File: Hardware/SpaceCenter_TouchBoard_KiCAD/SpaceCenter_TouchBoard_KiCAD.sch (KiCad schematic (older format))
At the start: 6 parts, among them J1 Conn_01x05_Male, J2 TOUCH_SENSOR

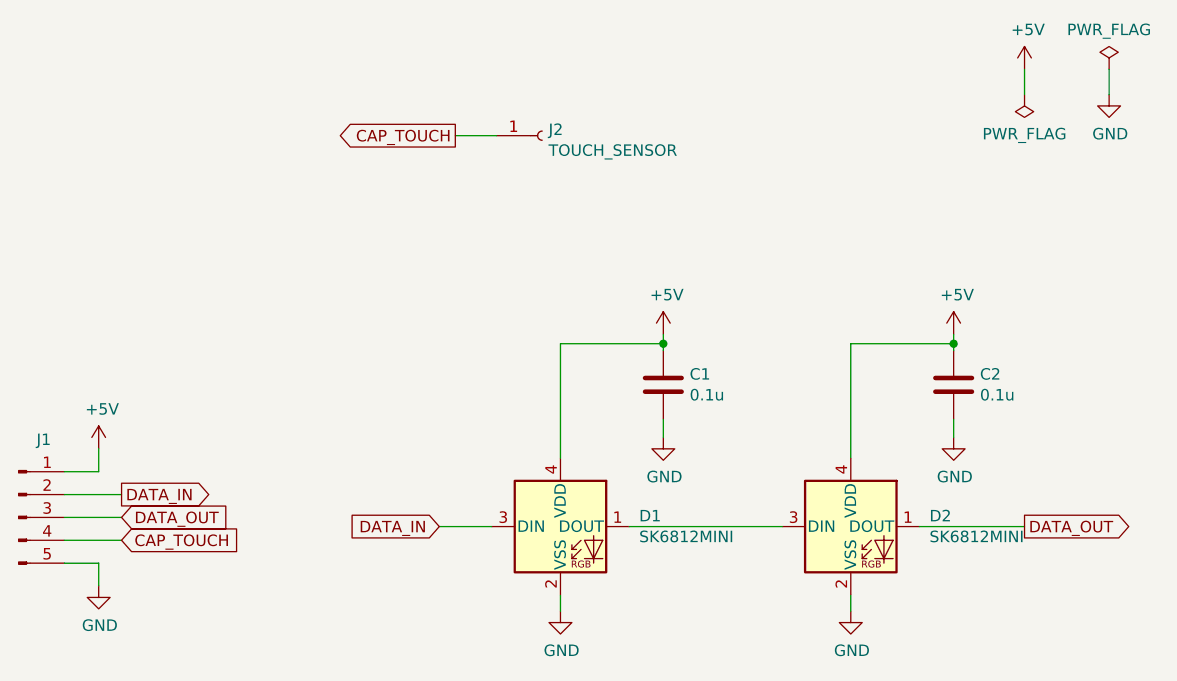
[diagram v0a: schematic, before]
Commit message: TouchBoard updated and ordered
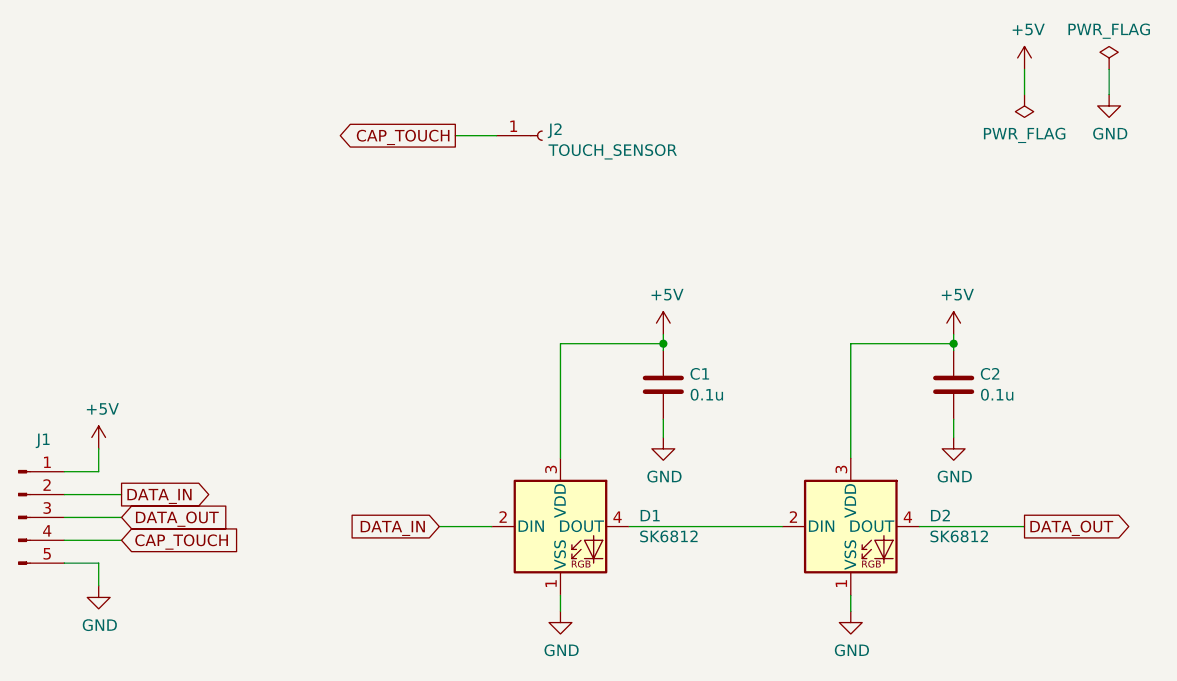
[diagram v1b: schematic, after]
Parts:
- removed D1, D2: SK6812MINI, LED_SMD:LED_SK6812MINI_PLCC4_3.5x3.5mm_P1.75mm, symbol LED:SK6812MINI
- added D1, D2: SK6812, LED_SMD:LED_SK6812_PLCC4_5.0x5.0mm_P3.2mm, symbol LED:SK6812
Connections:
- net +5V: now also D1.3 (VDD), D2.3 (VDD)
- net DATA_IN: now also D1.2 (DIN)
- net DATA_OUT: now also D2.4 (DOUT)
- net GND: now also D1.1 (VSS), D2.1 (VSS)
- new net: D1.4 (DOUT), D2.2 (DIN)
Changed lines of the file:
@@
 $EndDescr
-$Comp
-L LED:SK6812MINI D1
-U 1 1 5F27FCDA
-P 6030 4000
-F 0 "D1" H 6374 4046 50  0000 L CNN
-F 1 "SK6812MINI" H 6374 3955 50  0000 L CNN
-F 2 "LED_SMD:LED_SK6812MINI_PLCC4_3.5x3.5mm_P1.75mm" H 6080 3700 50  0001 L TNN
-F 3 "https://cdn-shop.adafruit.com/product-files/2686/SK6812MINI_REV.01-1-2.pdf" H 6130 3625 50  0001 L TNN
-	1    6030 4000
-	1    0    0    -1
-$EndComp
-$Comp
-L LED:SK6812MINI D2
-U 1 1 5F280339
-P 7300 4000
-F 0 "D2" H 7644 4046 50  0000 L CNN
-F 1 "SK6812MINI" H 7644 3955 50  0000 L CNN
-F 2 "LED_SMD:LED_SK6812MINI_PLCC4_3.5x3.5mm_P1.75mm" H 7350 3700 50  0001 L TNN
-F 3 "https://cdn-shop.adafruit.com/product-files/2686/SK6812MINI_REV.01-1-2.pdf" H 7400 3625 50  0001 L TNN
-	1    7300 4000
-	1    0    0    -1
-$EndComp
 $Comp
 L Device:C C1
@@
 Wire Wire Line
 	3860 3860 4110 3860
+$Comp
+L LED:SK6812 D2
+U 1 1 608949E1
+P 7300 4000
+F 0 "D2" H 7644 4046 50  0000 L CNN
+F 1 "SK6812" H 7644 3955 50  0000 L CNN
+F 2 "LED_SMD:LED_SK6812_PLCC4_5.0x5.0mm_P3.2mm" H 7350 3700 50  0001 L TNN
+F 3 "https://cdn-shop.adafruit.com/product-files/1138/SK6812+LED+datasheet+.pdf" H 7400 3625 50  0001 L TNN
+	1    7300 4000
+	1    0    0    -1
+$EndComp
+$Comp
+L LED:SK6812 D1
+U 1 1 60895375
+P 6030 4000
+F 0 "D1" H 6374 4046 50  0000 L CNN
+F 1 "SK6812" H 6374 3955 50  0000 L CNN
+F 2 "LED_SMD:LED_SK6812_PLCC4_5.0x5.0mm_P3.2mm" H 6080 3700 50  0001 L TNN
+F 3 "https://cdn-shop.adafruit.com/product-files/1138/SK6812+LED+datasheet+.pdf" H 6130 3625 50  0001 L TNN
+	1    6030 4000
+	1    0    0    -1
+$EndComp
 $EndSCHEMATC
